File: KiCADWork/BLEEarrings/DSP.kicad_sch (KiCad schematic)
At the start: 1 part, among them U5 ESP32-C3FH4

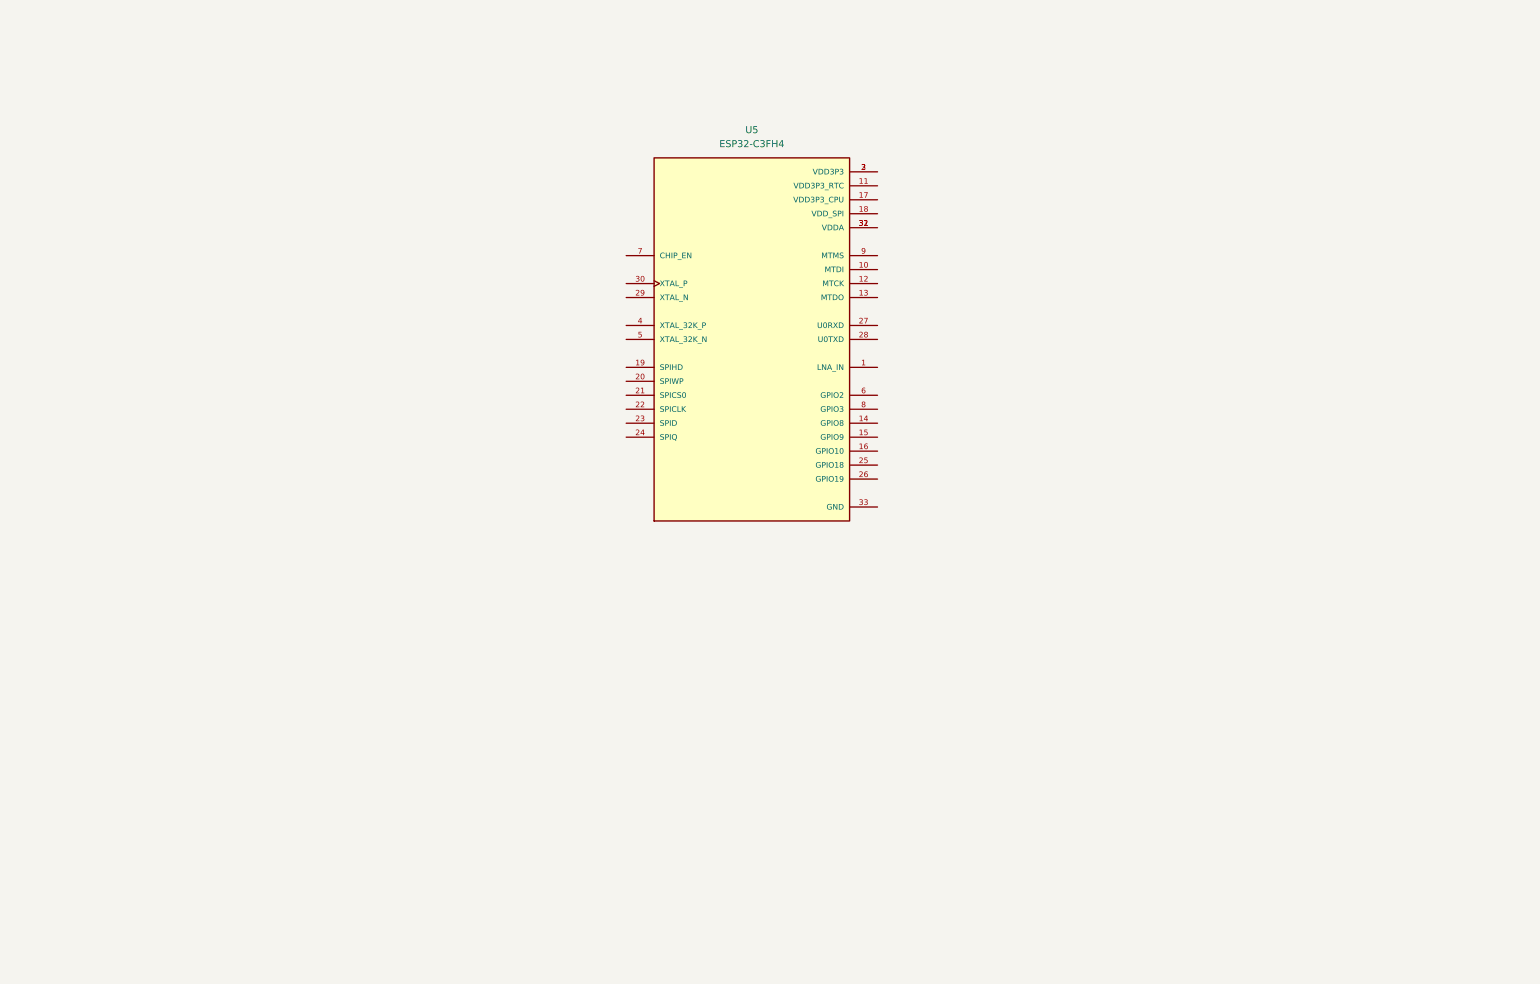
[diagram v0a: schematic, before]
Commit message: First Draft Schematic Done
- Symbols and footprints checked
- Dom added to repo
- Centralised footprints created
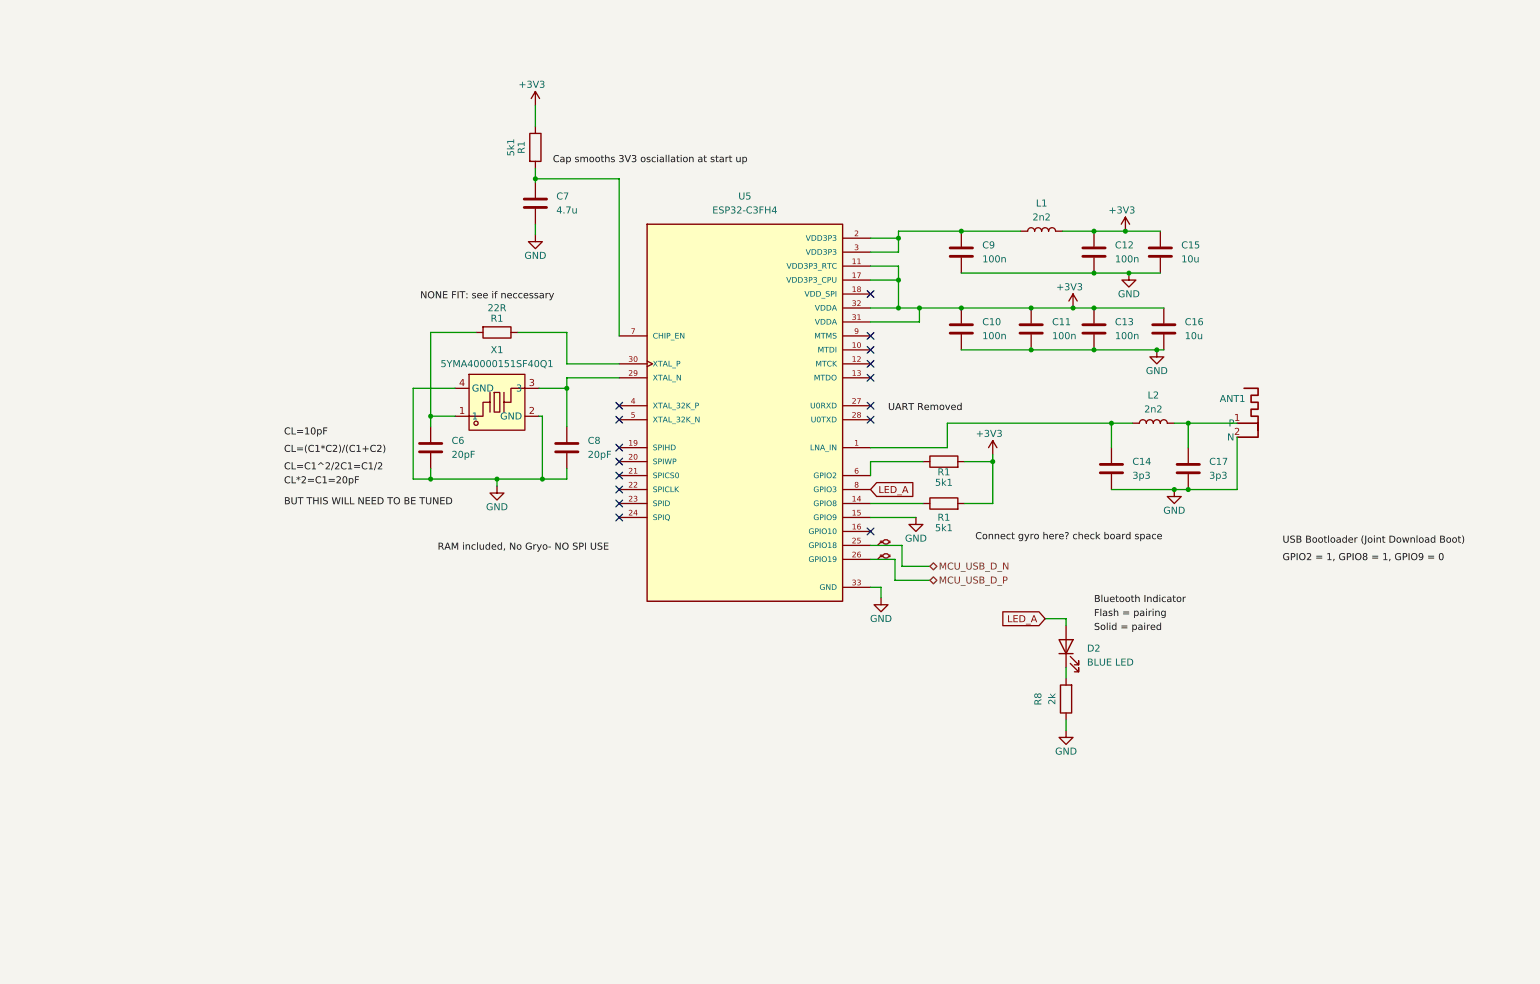
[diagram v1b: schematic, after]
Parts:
- added ANT1: ~, CustomPads:2.4GHz, 50Ohm Antenna, symbol CustomPads:2.4GHz,_50Ohm_Antenna
- added C10, C11, C12, C13, C9: 100n, Capacitor_SMD:C_0402_1005Metric_Pad0.74x0.62mm_HandSolder, symbol Device:C
- added C14, C17: 3p3, Capacitor_SMD:C_0402_1005Metric_Pad0.74x0.62mm_HandSolder, symbol Device:C
- added C15, C16: 10u, Capacitor_SMD:C_0402_1005Metric_Pad0.74x0.62mm_HandSolder, symbol Device:C
- added C6, C8: 20pF, Capacitor_SMD:C_0402_1005Metric_Pad0.74x0.62mm_HandSolder, symbol Device:C
- added C7: 4.7u, Capacitor_SMD:C_0402_1005Metric_Pad0.74x0.62mm_HandSolder, symbol Device:C
- added D2: BLUE LED, LED_SMD:LED_0603_1608Metric_Pad1.05x0.95mm_HandSolder, symbol Device:LED
- added L1, L2: 2n2, Inductor_SMD:L_0402_1005Metric_Pad0.77x0.64mm_HandSolder, symbol Device:L
- added MP4 (x2): ~, symbol CustomPads:Matched_Impedance
- added R1 (x3): 5k1, Resistor_SMD:R_0402_1005Metric_Pad0.72x0.64mm_HandSolder, symbol Device:R
- added R1: 22R, Resistor_SMD:R_0402_1005Metric_Pad0.72x0.64mm_HandSolder, symbol Device:R
- added R8: 2k, Resistor_SMD:R_0402_1005Metric_Pad0.72x0.64mm_HandSolder, symbol Device:R
- added X1: 5YMA40000151SF40Q1, easyeda2kicad:CRYSTAL-SMD_4P-L3.2-W2.5-BL, symbol easyeda2kicad:5YMA40000151SF40Q1
- U5: footprint ESP32-C3FH4:QFN50P500X500X90-33N -> easyeda2kicad:QFN-32_L5.0-W5.0-P0.50-TL-EP3.7
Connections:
- net at U5.1 (LNA_IN): now also C14.1, L2.1
- net +3V3: now reaches U5.11 (VDD3P3_RTC)
- net +3V3: now also U5.17 (VDD3P3_CPU), U5.31 (VDDA), U5.32 (VDDA), C10.1, C11.1, C12.1, C13.1, C15.1, C16.1, L1.2, R1.1, R1.2, R1.2
- net at U5.14 (GPIO8): now also R1.1
- net GND: now reaches U5.15 (GPIO9)
- net GND: now also U5.33 (GND), ANT1.2 (N), C10.2, C11.2, C12.2, C13.2, C14.2, C15.2, C16.2, C17.2, C6.2, C7.2, C8.2, C9.2, R8.1, X1.2 (GND), X1.4 (GND)
- net at U5.2 (VDD3P3), U5.3 (VDD3P3): now also C9.1, L1.1
- net MCU_USB_D_N: now reaches U5.25 (GPIO18)
- net MCU_USB_D_P: now reaches U5.26 (GPIO19)
- net at U5.29 (XTAL_N): now also C8.1, X1.3
- net at U5.30 (XTAL_P): now also R1.1
- net at U5.6 (GPIO2): now also R1.1
- net at U5.7 (CHIP_EN): now also C7.1, R1.2
- net LED_A: now reaches U5.8 (GPIO3)
- net LED_A: now also D2.2 (A)
- new net: C6.1, R1.2, X1.1
- new net: ANT1.1 (P), C17.1, L2.2
- new net: D2.1 (K), R8.2
- no-connect marks 0 -> 16
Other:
- company: (none) -> Kitty and Dom
- title: (none) -> BLEEarrings (Blade Runner)

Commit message: Improved Antenna Layout
- Initial layout complete
- TO DO:
    - Test points
    - Curved Tracks
    - Silkscreen
    - Check antenna
    - create casing in blender
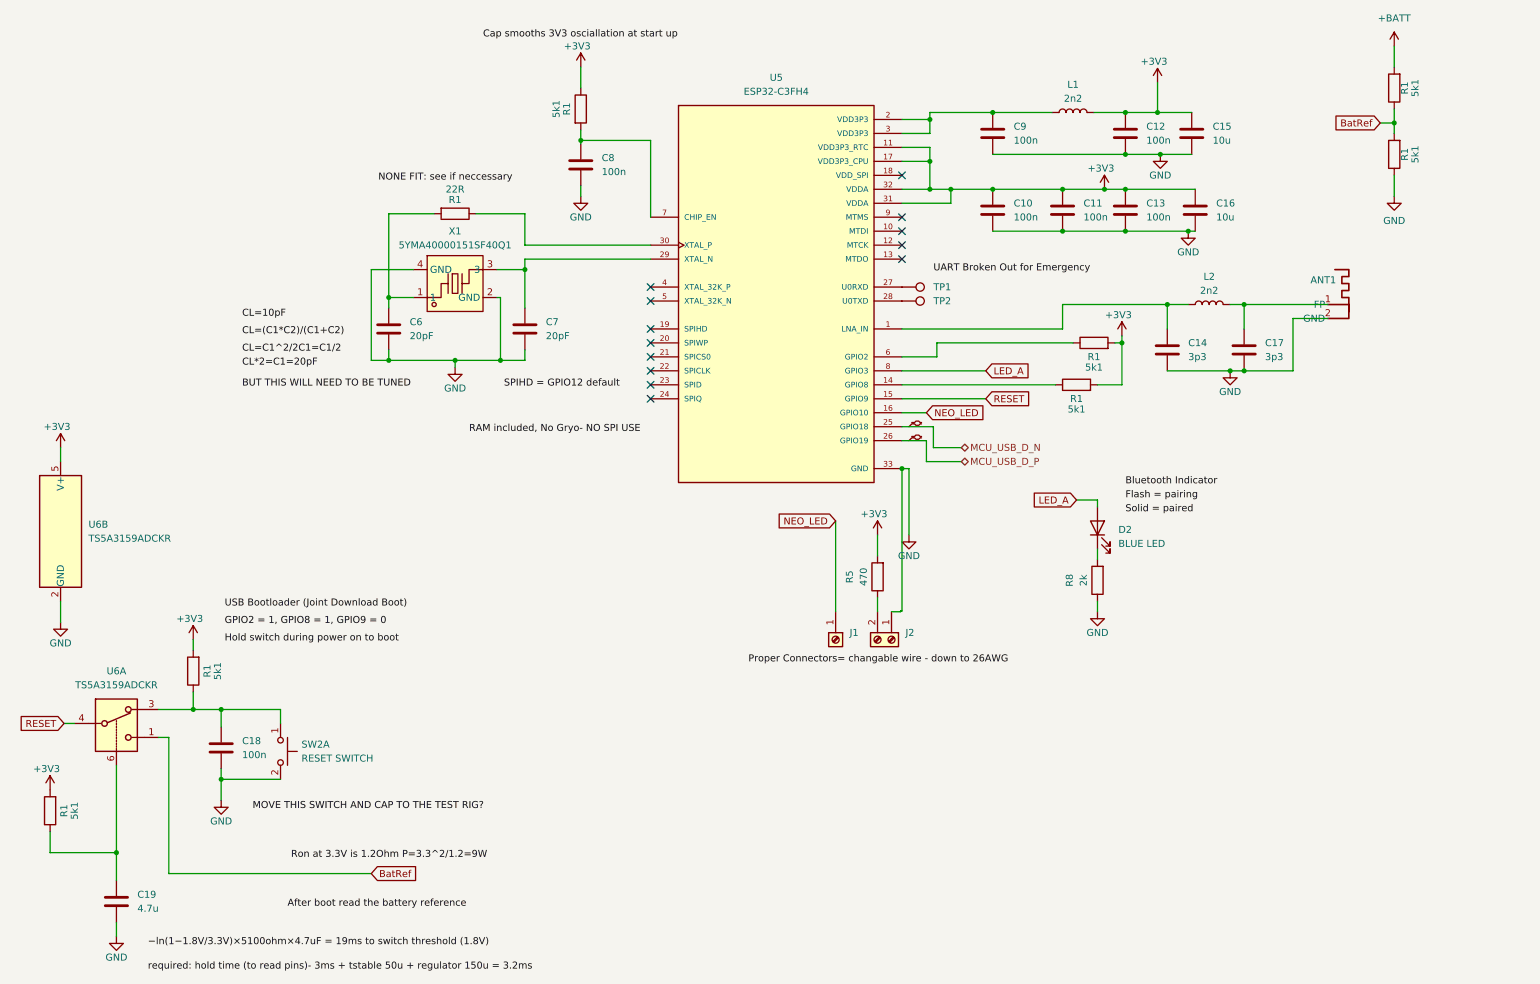
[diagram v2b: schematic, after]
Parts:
- added C18: 100n, Capacitor_SMD:C_0402_1005Metric_Pad0.74x0.62mm_HandSolder, symbol Device:C
- added C19: 4.7u, Capacitor_SMD:C_0402_1005Metric_Pad0.74x0.62mm_HandSolder, symbol Device:C
- added J1: Screw_Terminal_01x01, easyeda2kicad:CONN-SMD_custom1, symbol Connector:Screw_Terminal_01x01
- added J2: Screw_Terminal_01x02, easyeda2kicad:CONN-SMD_2059-302, symbol Connector:Screw_Terminal_01x02
- added R1 (x4): 5k1, Resistor_SMD:R_0402_1005Metric_Pad0.72x0.64mm_HandSolder, symbol Device:R
- added R5: 470, Resistor_SMD:R_0402_1005Metric_Pad0.72x0.64mm_HandSolder, symbol Device:R
- added SW2: RESET SWITCH, easyeda2kicad:SW-SMD_L3.9-W3.0-P4.45, symbol Switch:SW_Push_Dual_x2
- added TP1, TP2: TestPoint, TestPoint:TestPoint_Pad_2.0x2.0mm, symbol Connector:TestPoint
- added U6: TS5A3159ADCKR, Package_TO_SOT_SMD:SOT-363_SC-70-6, symbol Analog_Switch:TS5A3159ADCKR
- ANT1: footprint CustomPads:2.4GHz, 50Ohm Antenna -> RF_Antenna:Texas_SWRA117D_2.4GHz_Right
- C8: renamed from C7; value 4.7u -> 100n
- renumbered C8 to C7
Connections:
- net +3V3: now also R1.2, R1.2, R5.2, U6.5 (V+)
- net GND: now also C18.2, C19.2, J2.1 (Pin_1), R1.1, SW2.2 (D), U6.2 (GND); no longer U5.15 (GPIO9)
- net NEO_LED: now reaches U5.16 (GPIO10)
- net NEO_LED: now also J1.1 (Pin_1)
- net at U5.27 (U0RXD): now also TP1.1
- net at U5.28 (U0TXD): now also TP2.1
- new net: C19.1, R1.1, U6.6
- new net: C18.1, R1.1, SW2.1 (C), U6.3
- new net: J2.2 (Pin_2), R5.1
- new net +BATT: R1.2
- new net BatRef: R1.1, R1.2, U6.1
- new net RESET: U5.15 (GPIO9), U6.4
- no-connect marks 16 -> 13
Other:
- moved on the sheet: ANT1, C10, C11, C12, C13, C14, C15, C16, C17, C6, C7, C8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
